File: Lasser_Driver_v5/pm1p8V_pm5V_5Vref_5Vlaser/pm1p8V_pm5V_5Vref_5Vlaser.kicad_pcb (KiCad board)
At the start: 2 copper layers, 160 x 100 mm, 95 parts, among them J6 DIN41612_M_3x8+8_Power_Male, U1 MC7808CTG, U10 LT3042EMSE +14.3V, U13 MC7812CTG, U14 MC7808CTG, U15 LT3045EMSE 5V, U16 LT3045EMSE 5V, U17 MC7808CTG, U18 LM7905_TO220, U19 LT3045EMSE 5V, U2 LT3042EMSE +5.5V, U20 LT3094EMSE -5V, U21 OPA192IDBVR, U3 LTC6655BHMS8-5#PBF, U4 MC7812CTG, U5 MC7805CTG, U6 LT3045EMSE 3.3V, U7 LP5907MFX-1.8, U8 TPS7A3901DSCR, U9 LT3094EMSE -14.3V

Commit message: Continued work on power booards.
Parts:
- added C75: 1uF, Capacitor_SMD:C_0805_2012Metric_Pad1.18x1.45mm_HandSolder, F.Cu at (93.9, 136.8)
- added HS1: Heatsink Boyd 531102B02500G, Heatsink:Heatsink_AAVID_Extruded_531102B02500G_34.9x12.7mm_H38.1mm, F.Cu at (127.4, 68.0)
- added HS2: Heatsink Boyd 531102B02500G, Heatsink:Heatsink_AAVID_Extruded_531102B02500G_34.9x12.7mm_H38.1mm, F.Cu at (151.2, 68.0)
- added HS3: Heatsink Boyd 531102B02500G, Heatsink:Heatsink_AAVID_Extruded_531102B02500G_34.9x12.7mm_H38.1mm, F.Cu at (174.7, 68.0)
- added HS4: Heatsink Boyd 531102B02500G, Heatsink:Heatsink_AAVID_Extruded_531102B02500G_34.9x12.7mm_H38.1mm, F.Cu at (198.4, 68.0)
- added HS5: Heatsink Boyd 531102B02500G, Heatsink:Heatsink_AAVID_Extruded_531102B02500G_34.9x12.7mm_H38.1mm, F.Cu at (80.1, 68.0)
- added HS6: Heatsink Boyd 531102B02500G, Heatsink:Heatsink_AAVID_Extruded_531102B02500G_34.9x12.7mm_H38.1mm, F.Cu at (103.9, 68.0)
- added R50: 49.9R, Resistor_SMD:R_0805_2012Metric_Pad1.20x1.40mm_HandSolder, F.Cu at (89.2, 133.4)
- R10: value 54.9k 0.1% -> 60.4k 0.1%
- R11: value 1k -> 0R
- R15: value 12.7k 0.1% -> 137k 0.1%
- R16: value 1k -> 10k 0.1%
- R41: value 49.9k 0.1% -> 24.9k 0.1%
- R44: value 16k -> 604
- R48, R49: value 10k -> 10k 0.1%
- U18: value LM7905_TO220 -> MC7906CTG
- moved U18 132.7 mm to (202.6, 70.6), turned to 90 degrees
- moved U17 108.5 mm to (179.0, 70.6), turned to 90 degrees
- moved U10 91.2 mm to (76.5, 122.1), turned to 180 degrees
- moved U20 90.7 mm to (180.2, 104.1)
- moved R18 89.5 mm to (71.4, 123.6), turned to 180 degrees
- moved C18 86.1 mm to (111.4, 186.7)
- moved C22 86.1 mm to (116.2, 168.7)
- moved C54 86.1 mm to (121.0, 177.7)
- moved C57 86.1 mm to (121.0, 186.7)
- moved C61 86.1 mm to (125.8, 168.7)
- moved C64 86.1 mm to (125.8, 177.7)
- moved C67 86.1 mm to (125.8, 186.7)
- moved C70 86.1 mm to (130.6, 168.7)
- moved R43 86.1 mm to (140.2, 174.4)
- moved R45 86.1 mm to (140.2, 180.3)
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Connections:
- C59 pad 1: GND -> Net-(U15-EN/UV)
- R16 pad 2: GND -> Net-(U8-BUF)
- R40 pad 2: GND -> Net-(U15-EN/UV)
- R48 pad 2: +5V -> 5Vref
- R49 pad 1: -5V -> GND
- U15 pad 1: GND -> Net-(U15-EN/UV)
- U15 pad 2: GND -> Net-(U15-EN/UV)
- U15 pad 3: GND -> Net-(U15-EN/UV)
- U15 pad 4: GND -> Net-(U15-EN/UV)
- U15 pad 7: GND -> Net-(U15-EN/UV)
- U16 pad 1: GND -> Net-(U15-EN/UV)
- U16 pad 2: GND -> Net-(U15-EN/UV)
- U16 pad 3: GND -> Net-(U15-EN/UV)
- U16 pad 4: GND -> Net-(U15-EN/UV)
- U16 pad 7: GND -> Net-(U15-EN/UV)
- U21 pad 1: VREF_MID -> Net-(U21-IN-)
- U21 pad 2: VREF_MID -> Net-(U21-IN-)
- U8 pad 8: unconnected-(U8-BUF-Pad8)_1 -> Net-(U8-BUF)

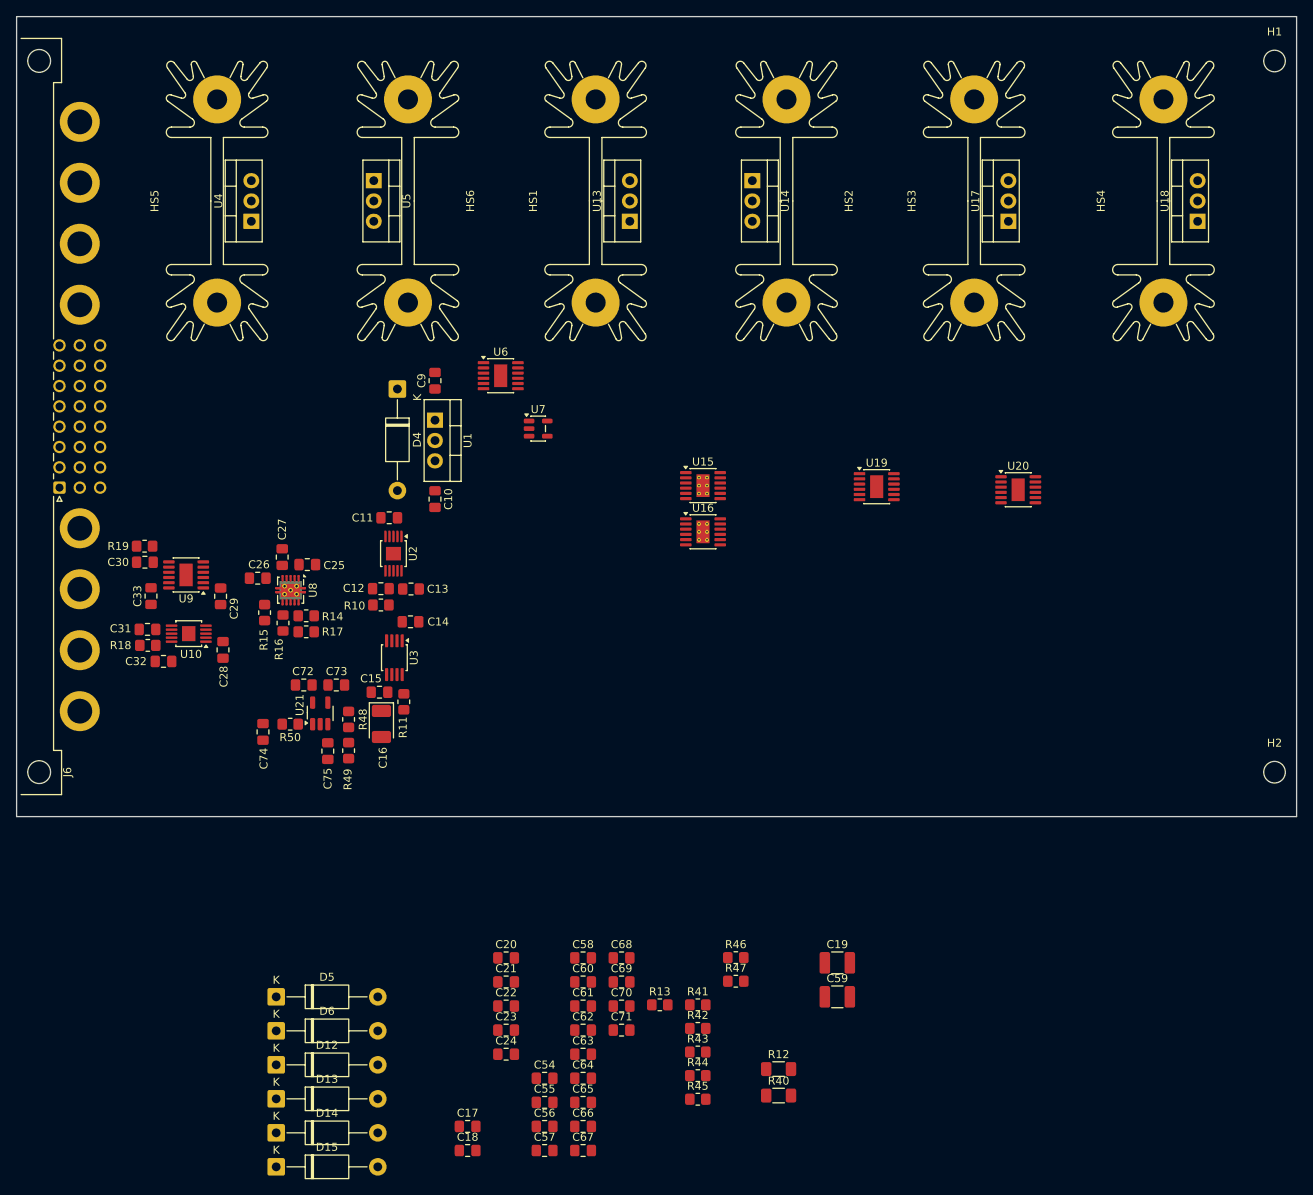
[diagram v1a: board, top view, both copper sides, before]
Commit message: Power cards should be done now.
This should be the last power card.  Need to do one last review, but routing seems to be good.
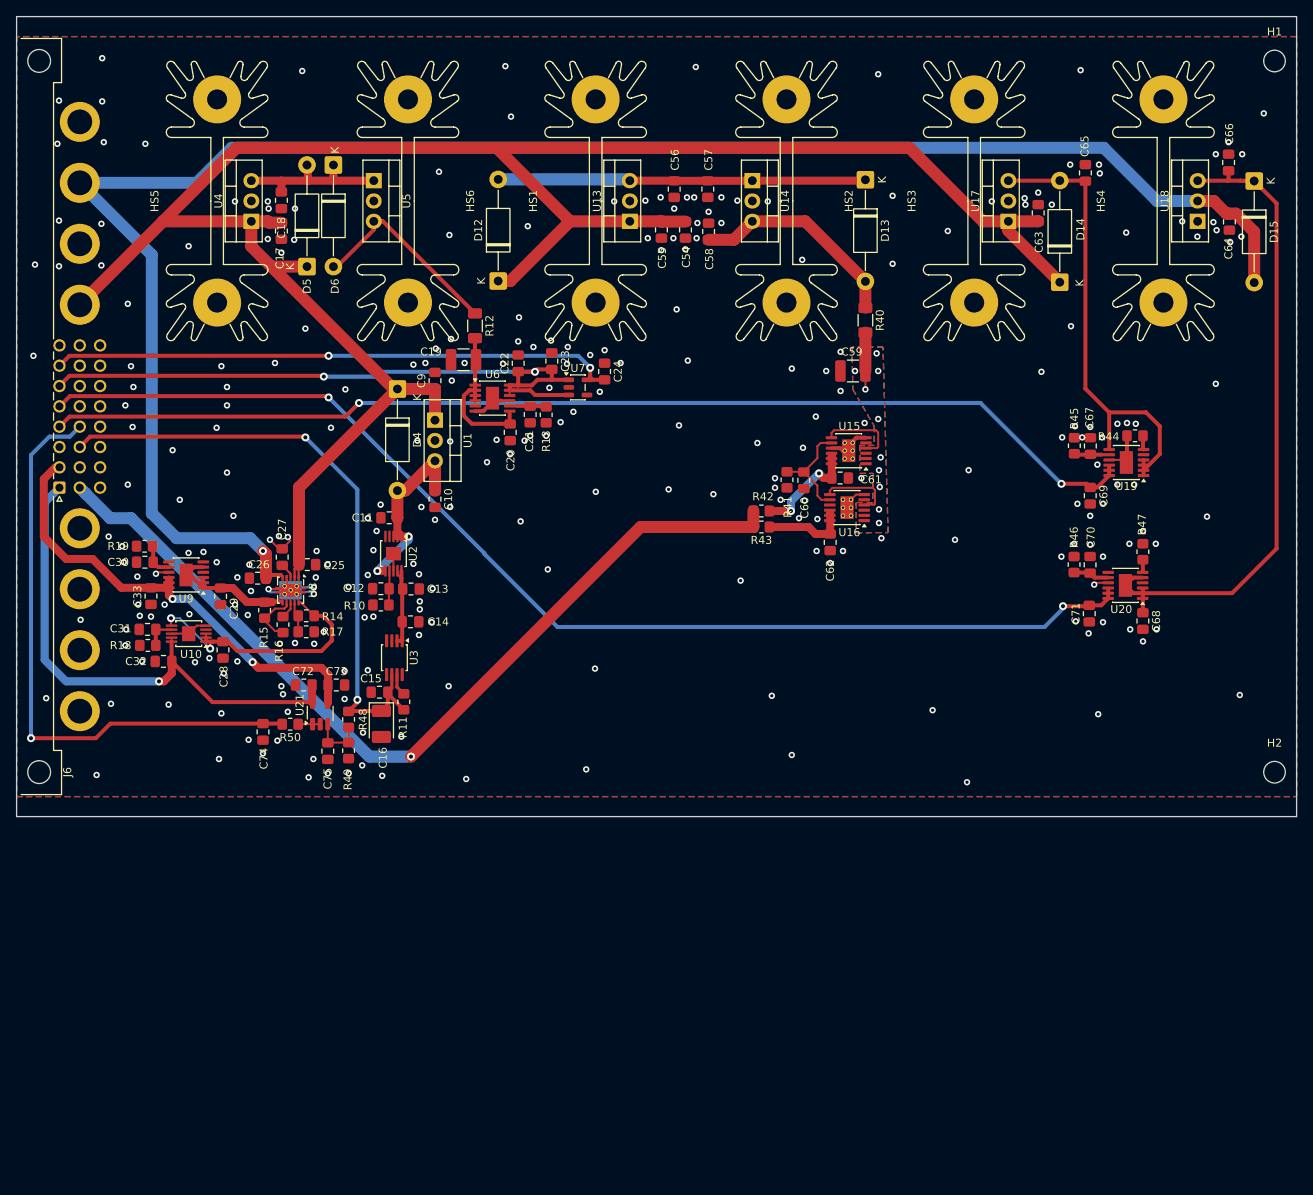
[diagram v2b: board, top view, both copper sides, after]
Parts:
- moved D15 173.6 mm to (209.7, 65.5), turned to -90 degrees
- moved C66 145.0 mm to (206.5, 63.2), turned to -90 degrees
- moved D14 144.6 mm to (185.4, 78.2), turned to 90 degrees
- moved D13 136.5 mm to (161.1, 65.4), turned to -90 degrees
- moved C64 134.1 mm to (206.6, 70.7), turned to 90 degrees
- moved C65 132.1 mm to (188.6, 64.5), turned to 90 degrees
- moved C57 121.9 mm to (141.4, 66.6), turned to -90 degrees
- moved C18 121.0 mm to (88.1, 68.0), turned to -90 degrees
- moved C63 119.6 mm to (182.7, 69.5), turned to 90 degrees
- moved C56 118.3 mm to (137.2, 66.6), turned to -90 degrees
- moved C17 114.3 mm to (88.1, 71.8), turned to -90 degrees
- moved C55 110.0 mm to (135.6, 71.7), turned to -90 degrees
- moved C67 108.5 mm to (189.2, 98.7), turned to 90 degrees
- moved D6 108.5 mm to (94.6, 63.5), turned to -90 degrees
- moved C54 107.5 mm to (138.6, 71.7), turned to -90 degrees
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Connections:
- J6 pad P2: DGND -> unconnected-(J6-PadP2)
- J6 pad P4: DGND -> unconnected-(J6-PadP4)
- J6 pad a20: DGND -> unconnected-(J6-Pada20)
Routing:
- net +18V: track 0.00 -> 269.0 mm
- net -18V: track 0.00 -> 226.3 mm, vias 0 -> 1
- net -5V: track 0.00 -> 146.5 mm, vias 0 -> 2
- net +5V: track 0.00 -> 138.6 mm, vias 0 -> 2
- net +5V_LASER: track 0.00 -> 112.0 mm, vias 0 -> 1
- net 3V3: track 0.00 -> 84.3 mm, vias 0 -> 2
- net Net-(D15-K): track 0.00 -> 83.6 mm
- net 5Vref: track 0.00 -> 78.4 mm, vias 0 -> 2
- net VREF_MID: track 0.00 -> 75.2 mm, vias 0 -> 1
- net 1V8: track 0.00 -> 71.3 mm, vias 0 -> 2
- net +15V: track 0.00 -> 66.1 mm, vias 0 -> 1
- net -15V: track 0.00 -> 59.9 mm, vias 0 -> 2
- net Net-(D14-A): track 0.00 -> 59.7 mm
- net GND: track 0.00 -> 51.6 mm, vias 0 -> 267
- net Net-(D12-A): track 0.00 -> 46.0 mm
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- added copper zone on B.Cu, net GND
- added copper zone on F.Cu, net GND
- added copper zone on B.Cu, net Net-(U15-EN/UV)
- added copper zone on F.Cu, net Net-(U15-EN/UV)
